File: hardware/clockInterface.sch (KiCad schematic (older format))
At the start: 9 parts, among them P501 CLOCK, SW501 SWITCH_INV, SW502 SWITCH_INV, SW503 SWITCH_INV, SW504 SWITCH_INV

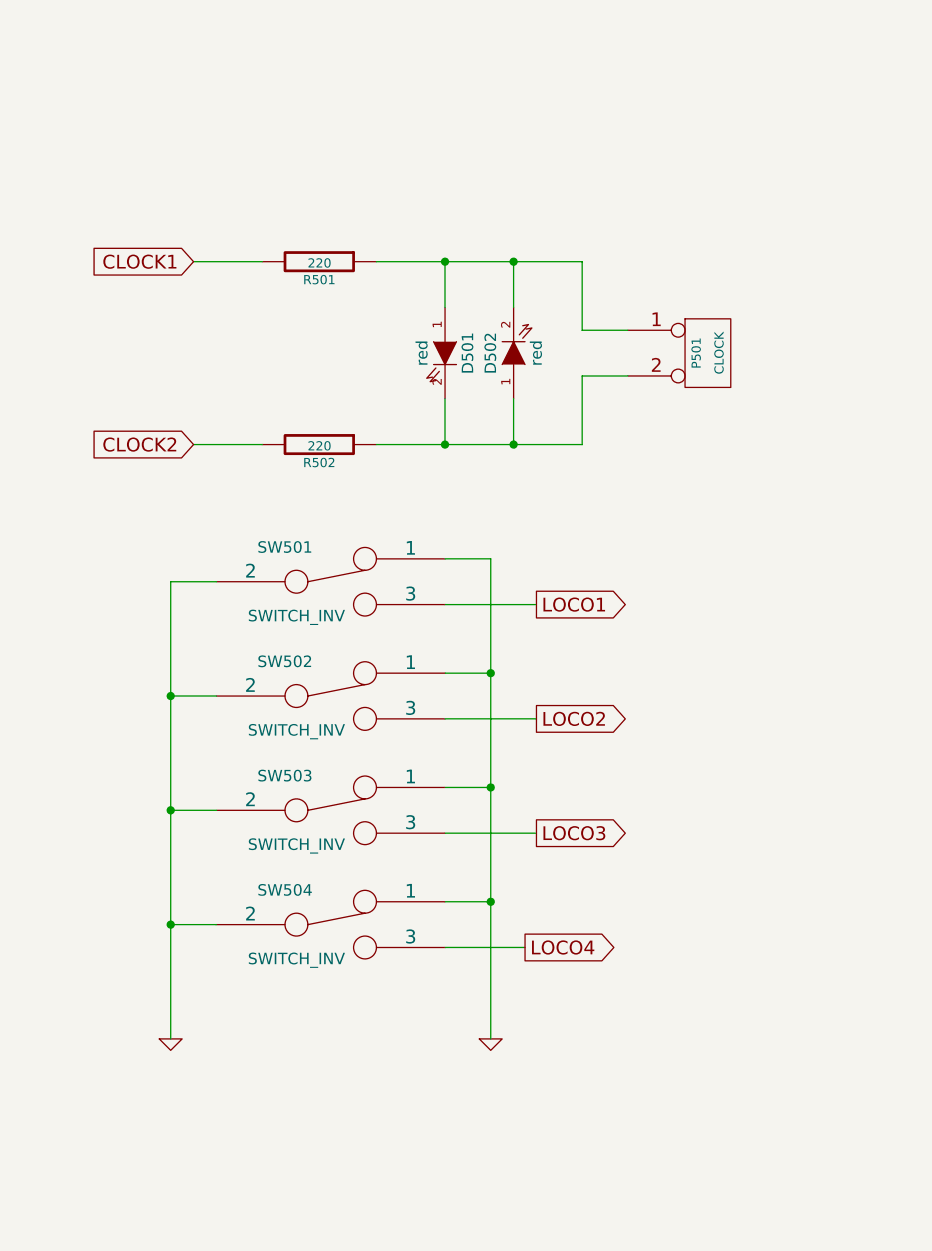
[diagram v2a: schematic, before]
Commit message: Change clock schematic and PCB
- Remove slide switches, replace with single push button
- Add status LED
- Re-add battery measurement connection

- Change PCB form factor to fit NewAgeEnclosures Compact AA housing
- Re-layout PCB
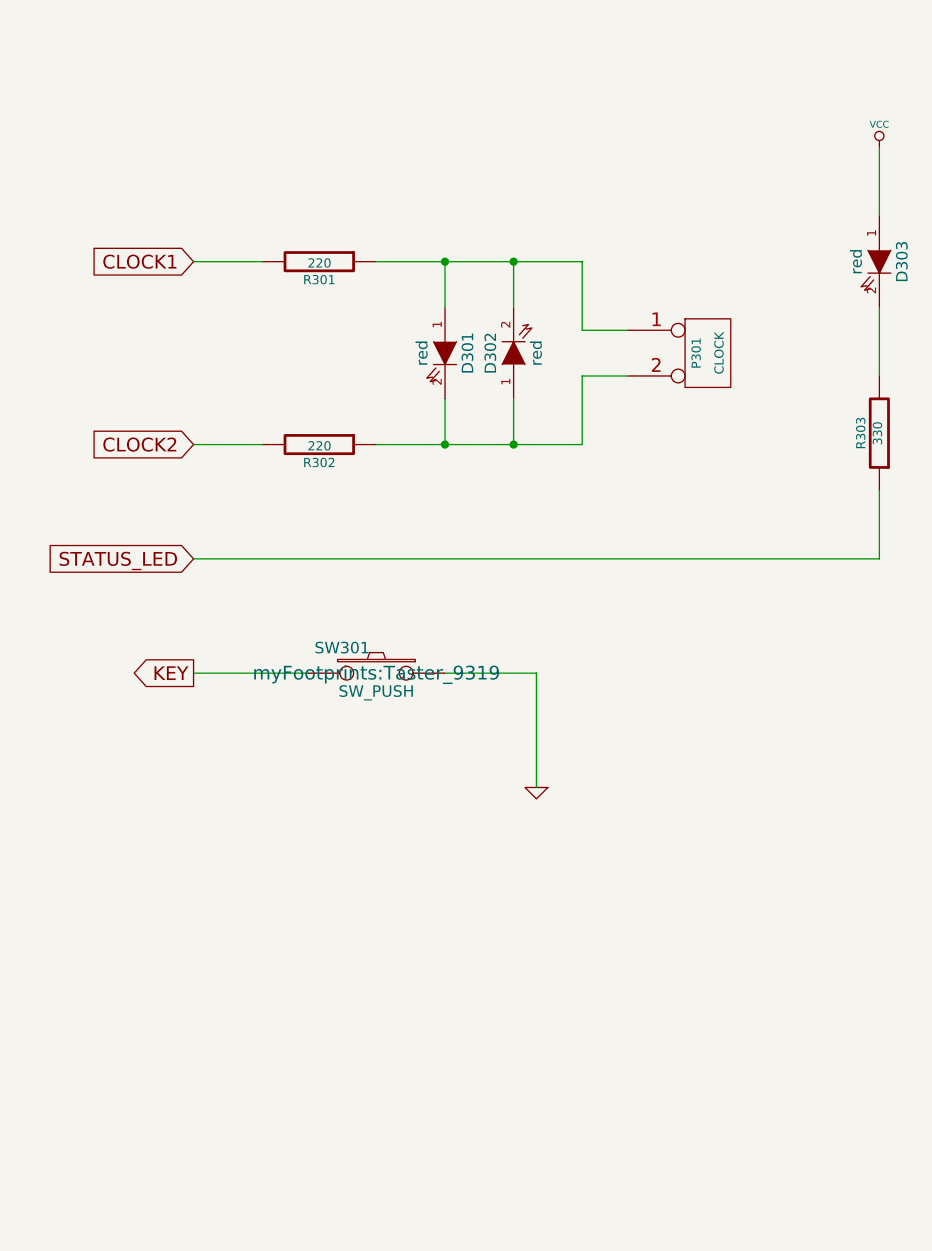
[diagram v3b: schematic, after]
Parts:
- removed SW501, SW502, SW503, SW504: SWITCH_INV, myFootprints:OS102011MS2Q, symbol SWITCH_INV
- added D303: red, myFootprints:LED_D3.0mm, symbol LED
- added R303: 330, Capacitors_SMD:C_0805_HandSoldering, symbol R
- added SW301: SW_PUSH, myFootprints:Taster_9319, symbol SW_PUSH
- renumbered D501 to D301, D502 to D302, P501 to P301, R501 to R301, R502 to R302
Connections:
- net GND: now also SW301.1
- new net: D303.2 (K), R303.2
- new net KEY: SW301.2
- new net STATUS_LED: R303.1
- new net VCC: D303.1 (A)
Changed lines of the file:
@@
 CLOCK2
 $Comp
-L R R501
+L R R301
 U 1 1 5A1291DD
 P 4450 2700
-F 0 "R501" V 4530 2700 40  0000 C CNN
+F 0 "R301" V 4530 2700 40  0000 C CNN
 F 1 "220" V 4457 2701 40  0000 C CNN
 F 2 "Capacitors_SMD:C_0805_HandSoldering" V 4380 2700 30  0001 C CNN
@@
 $EndComp
 $Comp
-L R R502
+L R R302
 U 1 1 5A12924F
 P 4450 3500
-F 0 "R502" V 4530 3500 40  0000 C CNN
+F 0 "R302" V 4530 3500 40  0000 C CNN
 F 1 "220" V 4457 3501 40  0000 C CNN
 F 2 "Capacitors_SMD:C_0805_HandSoldering" V 4380 3500 30  0001 C CNN
@@
 $EndComp
 $Comp
-L LED D501
+L LED D301
 U 1 1 5A12928F
 P 5000 3100
-F 0 "D501" H 5000 3200 50  0000 C CNN
+F 0 "D301" H 5000 3200 50  0000 C CNN
 F 1 "red" H 5000 3000 50  0000 C CNN
 F 2 "myFootprints:LED_D3.0mm" H 5000 3100 60  0001 C CNN
@@
 $EndComp
 $Comp
-L LED D502
+L LED D302
 U 1 1 5A129325
 P 5300 3100
-F 0 "D502" H 5300 3200 50  0000 C CNN
+F 0 "D302" H 5300 3200 50  0000 C CNN
 F 1 "red" H 5300 3000 50  0000 C CNN
 F 2 "myFootprints:LED_D3.0mm" H 5300 3100 60  0001 C CNN
@@
 $EndComp
 $Comp
-L CONN_2 P501
+L CONN_2 P301
 U 1 1 5A12938D
 P 6150 3100
-F 0 "P501" V 6100 3100 40  0000 C CNN
+F 0 "P301" V 6100 3100 40  0000 C CNN
 F 1 "CLOCK" V 6200 3100 40  0000 C CNN
 F 2 "myFootprints:AKL183-02" H 6150 3100 60  0001 C CNN
@@
 Connection ~ 5000 3500
 $Comp
-L SWITCH_INV SW501
-U 1 1 5A15342E
-P 4500 4100
-F 0 "SW501" H 4300 4250 50  0000 C CNN
-F 1 "SWITCH_INV" H 4350 3950 50  0000 C CNN
-F 2 "myFootprints:OS102011MS2Q" H 4500 4100 60  0001 C CNN
-F 3 "" H 4500 4100 60  0000 C CNN
-F 4 "611-OS102011MS2QN1" H 4500 4100 60  0001 C CNN "Mouser"
-	1    4500 4100
-	1    0    0    -1
+L GND #PWR018
+U 1 1 5A15360C
+P 5400 5000
+F 0 "#PWR018" H 5400 5000 30  0001 C CNN
+F 1 "GND" H 5400 4930 30  0001 C CNN
+F 2 "" H 5400 5000 60  0001 C CNN
+F 3 "" H 5400 5000 60  0001 C CNN
+	1    5400 5000
+	-1   0    0    -1
+$EndComp
+Wire Wire Line
+	5400 4500 5000 4500
+Text GLabel 3900 4500 0    60   Output ~ 0
+KEY
+Wire Wire Line
+	4400 4500 3900 4500
+Wire Wire Line
+	5400 4500 5400 5000
+$Comp
+L SW_PUSH SW301
+U 1 1 5C82A486
+P 4700 4500
+F 0 "SW301" H 4850 4610 50  0000 C CNN
+F 1 "SW_PUSH" H 4700 4420 50  0000 C CNN
+F 2 "myFootprints:Taster_9319" H 4700 4500 60  0000 C CNN
+F 3 "" H 4700 4500 60  0000 C CNN
+	1    4700 4500
+	-1   0    0    -1
 $EndComp
 $Comp
-L SWITCH_INV SW502
-U 1 1 5A15348B
-P 4500 4600
-F 0 "SW502" H 4300 4750 50  0000 C CNN
-F 1 "SWITCH_INV" H 4350 4450 50  0000 C CNN
-F 2 "myFootprints:OS102011MS2Q" H 4500 4600 60  0001 C CNN
-F 3 "" H 4500 4600 60  0000 C CNN
-F 4 "611-OS102011MS2QN1" H 4500 4600 60  0001 C CNN "Mouser"
-	1    4500 4600
-	1    0    0    -1
+L LED D303
+U 1 1 5C82A97E
+P 6900 2700
+F 0 "D303" H 6900 2800 50  0000 C CNN
+F 1 "red" H 6900 2600 50  0000 C CNN
+F 2 "myFootprints:LED_D3.0mm" H 6900 2700 60  0001 C CNN
+F 3 "" H 6900 2700 60  0000 C CNN
+F 4 "LED 3MM RT" H 6900 2700 60  0001 C CNN "Reichelt"
+	1    6900 2700
+	0    1    1    0
 $EndComp
 $Comp
-L SWITCH_INV SW503
-U 1 1 5A153526
-P 4500 5100
-F 0 "SW503" H 4300 5250 50  0000 C CNN
-F 1 "SWITCH_INV" H 4350 4950 50  0000 C CNN
-F 2 "myFootprints:OS102011MS2Q" H 4500 5100 60  0001 C CNN
-F 3 "" H 4500 5100 60  0000 C CNN
-F 4 "611-OS102011MS2QN1" H 4500 5100 60  0001 C CNN "Mouser"
-	1    4500 5100
-	1    0    0    -1
+L R R303
+U 1 1 5C82AAA2
+P 6900 3450
+F 0 "R303" V 6980 3450 40  0000 C CNN
+F 1 "330" V 6907 3451 40  0000 C CNN
+F 2 "Capacitors_SMD:C_0805_HandSoldering" V 6830 3450 30  0001 C CNN
+F 3 "" H 6900 3450 30  0000 C CNN
+F 4 "603-RC0805JR-07220RL" V 6900 3450 60  0001 C CNN "Mouser"
+	1    6900 3450
+	-1   0    0    1
 $EndComp
 $Comp
-L SWITCH_INV SW504
-U 1 1 5A1535A1
-P 4500 5600
-F 0 "SW504" H 4300 5750 50  0000 C CNN
-F 1 "SWITCH_INV" H 4350 5450 50  0000 C CNN
-F 2 "myFootprints:OS102011MS2Q" H 4500 5600 60  0001 C CNN
-F 3 "" H 4500 5600 60  0000 C CNN
-F 4 "611-OS102011MS2QN1" H 4500 5600 60  0001 C CNN "Mouser"
-	1    4500 5600
-	1    0    0    -1
-$EndComp
-$Comp
-L GND #PWR017
-U 1 1 5A15360C
-P 3800 6100
-F 0 "#PWR017" H 3800 6100 30  0001 C CNN
-F 1 "GND" H 3800 6030 30  0001 C CNN
-F 2 "" H 3800 6100 60  0001 C CNN
-F 3 "" H 3800 6100 60  0001 C CNN
-	1    3800 6100
-	1    0    0    -1
-$EndComp
-$Comp
-L GND #PWR018
-U 1 1 5A15363B
-P 5200 6100
-F 0 "#PWR018" H 5200 6100 30  0001 C CNN
-F 1 "GND" H 5200 6030 30  0001 C CNN
-F 2 "" H 5200 6100 60  0001 C CNN
-F 3 "" H 5200 6100 60  0001 C CNN
-	1    5200 6100
+L VCC #PWR019
+U 1 1 5C82ABFF
+P 6900 2200
+F 0 "#PWR019" H 6900 2300 30  0001 C CNN
+F 1 "VCC" H 6900 2300 30  0000 C CNN
+F 2 "" H 6900 2200 60  0001 C CNN
+F 3 "" H 6900 2200 60  0001 C CNN
+	1    6900 2200
 	1    0    0    -1
 $EndComp
 Wire Wire Line
-	5200 6100 5200 4000
+	6900 2200 6900 2500
 Wire Wire Line
-	5200 4000 5000 4000
+	6900 2900 6900 3200
 Wire Wire Line
-	5000 4500 5200 4500
-Connection ~ 5200 4500
+	6900 3700 6900 4000
 Wire Wire Line
-	5000 5000 5200 5000
-Connection ~ 5200 5000
-Wire Wire Line
-	5000 5500 5200 5500
-Connection ~ 5200 5500
-Wire Wire Line
-	3800 4100 3800 6100
-Wire Wire Line
-	3800 5600 4000 5600
-Wire Wire Line
-	3800 5100 4000 5100
-Connection ~ 3800 5600
-Wire Wire Line
-	3800 4600 4000 4600
-Connection ~ 3800 5100
-Wire Wire Line
-	3800 4100 4000 4100
-Connection ~ 3800 4600
-Text GLabel 5400 4200 2    60   Output ~ 0
-LOCO1
-Text GLabel 5400 4700 2    60   Output ~ 0
-LOCO2
-Text GLabel 5400 5200 2    60   Output ~ 0
-LOCO3
-Text GLabel 5350 5700 2    60   Output ~ 0
-LOCO4
-Wire Wire Line
-	5400 4700 5000 4700
-Wire Wire Line
-	5000 4200 5400 4200
-Wire Wire Line
-	5400 5200 5000 5200
-Wire Wire Line
-	5000 5700 5350 5700
+	6900 4000 3900 4000
+Text GLabel 3900 4000 0    60   Input ~ 0
+STATUS_LED
 $EndSCHEMATC

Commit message: Changed PCB and code to closer match first PCB
- Add battery measurement resistors
- Move key, status LED and clock I/O-pins around to match first PCB
  (except for CLOCK1 which is on low power pin in first version)
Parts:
- SW301: Mouser (none) -> 611-PTS645SM13SMTR92
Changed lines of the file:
@@
 Connection ~ 5000 3500
 $Comp
-L GND #PWR018
+L GND #PWR019
 U 1 1 5A15360C
 P 5400 5000
-F 0 "#PWR018" H 5400 5000 30  0001 C CNN
+F 0 "#PWR019" H 5400 5000 30  0001 C CNN
 F 1 "GND" H 5400 4930 30  0001 C CNN
 F 2 "" H 5400 5000 60  0001 C CNN
@@
 F 2 "myFootprints:Taster_9319" H 4700 4500 60  0000 C CNN
 F 3 "" H 4700 4500 60  0000 C CNN
+F 4 "611-PTS645SM13SMTR92" H 4700 4500 60  0001 C CNN "Mouser"
 	1    4700 4500
 	-1   0    0    -1
@@
 $EndComp
 $Comp
-L VCC #PWR019
+L VCC #PWR020
 U 1 1 5C82ABFF
 P 6900 2200
-F 0 "#PWR019" H 6900 2300 30  0001 C CNN
+F 0 "#PWR020" H 6900 2300 30  0001 C CNN
 F 1 "VCC" H 6900 2300 30  0000 C CNN
 F 2 "" H 6900 2200 60  0001 C CNN

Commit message: Added more keys to the PCB for adjusting the time
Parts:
- added SW302, SW303, SW304: SW_PUSH, myFootprints:Taster_9319, symbol SW_PUSH
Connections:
- net GND: now also SW302.1, SW303.1, SW304.1
- net KEY: now also SW304.2; no longer SW301.2
- new net KEY_CONF: SW301.2
- new net KEY_HOUR: SW302.2
- new net KEY_MINUTE: SW303.2
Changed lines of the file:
@@
 L GND #PWR019
 U 1 1 5A15360C
-P 5400 5000
-F 0 "#PWR019" H 5400 5000 30  0001 C CNN
-F 1 "GND" H 5400 4930 30  0001 C CNN
-F 2 "" H 5400 5000 60  0001 C CNN
-F 3 "" H 5400 5000 60  0001 C CNN
-	1    5400 5000
+P 5400 6900
+F 0 "#PWR019" H 5400 6900 30  0001 C CNN
+F 1 "GND" H 5400 6830 30  0001 C CNN
+F 2 "" H 5400 6900 60  0001 C CNN
+F 3 "" H 5400 6900 60  0001 C CNN
+	1    5400 6900
 	-1   0    0    -1
 $EndComp
@@
 	5400 4500 5000 4500
 Text GLabel 3900 4500 0    60   Output ~ 0
-KEY
+KEY_CONF
 Wire Wire Line
 	4400 4500 3900 4500
 Wire Wire Line
-	5400 4500 5400 5000
+	5400 4500 5400 6900
 $Comp
 L SW_PUSH SW301
@@
 Text GLabel 3900 4000 0    60   Input ~ 0
 STATUS_LED
+Wire Wire Line
+	5400 4900 5000 4900
+Text GLabel 3900 4900 0    60   Output ~ 0
+KEY_HOUR
+Wire Wire Line
+	4400 4900 3900 4900
+$Comp
+L SW_PUSH SW302
+U 1 1 5CA9E853
+P 4700 4900
+F 0 "SW302" H 4850 5010 50  0000 C CNN
+F 1 "SW_PUSH" H 4700 4820 50  0000 C CNN
+F 2 "myFootprints:Taster_9319" H 4700 4900 60  0000 C CNN
+F 3 "" H 4700 4900 60  0000 C CNN
+F 4 "611-PTS645SM13SMTR92" H 4700 4900 60  0001 C CNN "Mouser"
+	1    4700 4900
+	-1   0    0    -1
+$EndComp
+Wire Wire Line
+	5400 5300 5000 5300
+Text GLabel 3900 5300 0    60   Output ~ 0
+KEY_MINUTE
+Wire Wire Line
+	4400 5300 3900 5300
+$Comp
+L SW_PUSH SW303
+U 1 1 5CA9E95A
+P 4700 5300
+F 0 "SW303" H 4850 5410 50  0000 C CNN
+F 1 "SW_PUSH" H 4700 5220 50  0000 C CNN
+F 2 "myFootprints:Taster_9319" H 4700 5300 60  0000 C CNN
+F 3 "" H 4700 5300 60  0000 C CNN
+F 4 "611-PTS645SM13SMTR92" H 4700 5300 60  0001 C CNN "Mouser"
+	1    4700 5300
+	-1   0    0    -1
+$EndComp
+Wire Wire Line
+	5400 5700 5000 5700
+Text GLabel 3900 5700 0    60   Output ~ 0
+KEY
+Wire Wire Line
+	4400 5700 3900 5700
+$Comp
+L SW_PUSH SW304
+U 1 1 5CA9E9B6
+P 4700 5700
+F 0 "SW304" H 4850 5810 50  0000 C CNN
+F 1 "SW_PUSH" H 4700 5620 50  0000 C CNN
+F 2 "myFootprints:Taster_9319" H 4700 5700 60  0000 C CNN
+F 3 "" H 4700 5700 60  0000 C CNN
+F 4 "611-PTS645SM13SMTR92" H 4700 5700 60  0001 C CNN "Mouser"
+	1    4700 5700
+	-1   0    0    -1
+$EndComp
+Connection ~ 5400 4900
+Connection ~ 5400 5300
+Connection ~ 5400 5700
 $EndSCHEMATC

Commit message: Add second clock output...
...while removing (so far) unused key
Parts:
- removed SW304: SW_PUSH, myFootprints:Taster_9319, symbol SW_PUSH
- added D304, D305: red, myFootprints:LED_D3.0mm, symbol LED
- added P302: CLOCK2, myFootprints:AKL183-02, symbol CONN_2
- added R304, R305: 220, Capacitors_SMD:C_0805_HandSoldering, symbol R
- D303: value red -> green
- P301: value CLOCK -> CLOCK1
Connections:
- new net: D304.1 (A), D305.2 (K), P302.1 (P1), R304.1
- new net: D304.2 (K), D305.1 (A), P302.2 (PM), R305.1
- new net CLOCK3: R304.2
- new net CLOCK4: R305.2
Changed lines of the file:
@@
 EESchema Schematic File Version 2
+LIBS:wfred_loconet_clock-rescue
 LIBS:power
 LIBS:device
@@
 P 6150 3100
 F 0 "P301" V 6100 3100 40  0000 C CNN
-F 1 "CLOCK" V 6200 3100 40  0000 C CNN
+F 1 "CLOCK1" V 6200 3100 40  0000 C CNN
 F 2 "myFootprints:AKL183-02" H 6150 3100 60  0001 C CNN
 F 3 "" H 6150 3100 60  0001 C CNN
@@
 Connection ~ 5000 3500
 $Comp
-L GND #PWR019
+L GND #PWR020
 U 1 1 5A15360C
 P 5400 6900
-F 0 "#PWR019" H 5400 6900 30  0001 C CNN
+F 0 "#PWR020" H 5400 6900 30  0001 C CNN
 F 1 "GND" H 5400 6830 30  0001 C CNN
 F 2 "" H 5400 6900 60  0001 C CNN
@@
 Wire Wire Line
 	4400 4500 3900 4500
-Wire Wire Line
-	5400 4500 5400 6900
 $Comp
 L SW_PUSH SW301
@@
 P 6900 2700
 F 0 "D303" H 6900 2800 50  0000 C CNN
-F 1 "red" H 6900 2600 50  0000 C CNN
+F 1 "green" H 6900 2600 50  0000 C CNN
 F 2 "myFootprints:LED_D3.0mm" H 6900 2700 60  0001 C CNN
 F 3 "" H 6900 2700 60  0000 C CNN
@@
 $EndComp
 $Comp
-L VCC #PWR020
+L VCC #PWR021
 U 1 1 5C82ABFF
 P 6900 2200
-F 0 "#PWR020" H 6900 2300 30  0001 C CNN
+F 0 "#PWR021" H 6900 2300 30  0001 C CNN
 F 1 "VCC" H 6900 2300 30  0000 C CNN
 F 2 "" H 6900 2200 60  0001 C CNN
@@
 	-1   0    0    -1
 $EndComp
-Wire Wire Line
-	5400 5700 5000 5700
-Text GLabel 3900 5700 0    60   Output ~ 0
-KEY
-Wire Wire Line
-	4400 5700 3900 5700
-$Comp
-L SW_PUSH SW304
-U 1 1 5CA9E9B6
-P 4700 5700
-F 0 "SW304" H 4850 5810 50  0000 C CNN
-F 1 "SW_PUSH" H 4700 5620 50  0000 C CNN
-F 2 "myFootprints:Taster_9319" H 4700 5700 60  0000 C CNN
-F 3 "" H 4700 5700 60  0000 C CNN
-F 4 "611-PTS645SM13SMTR92" H 4700 5700 60  0001 C CNN "Mouser"
-	1    4700 5700
-	-1   0    0    -1
-$EndComp
 Connection ~ 5400 4900
 Connection ~ 5400 5300
-Connection ~ 5400 5700
+Text GLabel 3900 1700 0    60   Input ~ 0
+CLOCK3
+Text GLabel 3900 2500 0    60   Input ~ 0
+CLOCK4
+$Comp
+L R R304
+U 1 1 5D44BDE6
+P 4450 1700
+F 0 "R304" V 4530 1700 40  0000 C CNN
+F 1 "220" V 4457 1701 40  0000 C CNN
+F 2 "Capacitors_SMD:C_0805_HandSoldering" V 4380 1700 30  0001 C CNN
+F 3 "" H 4450 1700 30  0000 C CNN
+F 4 "603-RC0805JR-07220RL" V 4450 1700 60  0001 C CNN "Mouser"
+	1    4450 1700
+	0    1    1    0
+$EndComp
+$Comp
+L R R305
+U 1 1 5D44BDED
+P 4450 2500
+F 0 "R305" V 4530 2500 40  0000 C CNN
+F 1 "220" V 4457 2501 40  0000 C CNN
+F 2 "Capacitors_SMD:C_0805_HandSoldering" V 4380 2500 30  0001 C CNN
+F 3 "" H 4450 2500 30  0000 C CNN
+F 4 "603-RC0805JR-07220RL" V 4450 2500 60  0001 C CNN "Mouser"
+	1    4450 2500
+	0    1    1    0
+$EndComp
+$Comp
+L LED D304
+U 1 1 5D44BDF4
+P 5000 2100
+F 0 "D304" H 5000 2200 50  0000 C CNN
+F 1 "red" H 5000 2000 50  0000 C CNN
+F 2 "myFootprints:LED_D3.0mm" H 5000 2100 60  0001 C CNN
+F 3 "" H 5000 2100 60  0000 C CNN
+F 4 "LED 3MM RT" H 5000 2100 60  0001 C CNN "Reichelt"
+	1    5000 2100
+	0    1    1    0
+$EndComp
+$Comp
+L LED D305
+U 1 1 5D44BDFB
+P 5300 2100
+F 0 "D305" H 5300 2200 50  0000 C CNN
+F 1 "red" H 5300 2000 50  0000 C CNN
+F 2 "myFootprints:LED_D3.0mm" H 5300 2100 60  0001 C CNN
+F 3 "" H 5300 2100 60  0000 C CNN
+F 4 "LED 3MM RT" H 5300 2100 60  0001 C CNN "Reichelt"
+	1    5300 2100
+	0    -1   -1   0
+$EndComp
+$Comp
+L CONN_2 P302
+U 1 1 5D44BE02
+P 6150 2100
+F 0 "P302" V 6100 2100 40  0000 C CNN
+F 1 "CLOCK2" V 6200 2100 40  0000 C CNN
+F 2 "myFootprints:AKL183-02" H 6150 2100 60  0001 C CNN
+F 3 "" H 6150 2100 60  0001 C CNN
+F 4 "AKL182-02 + AKL169-02" V 6150 2100 60  0001 C CNN "Reichelt"
+	1    6150 2100
+	1    0    0    -1
+$EndComp
+Wire Wire Line
+	3900 1700 4200 1700
+Wire Wire Line
+	4700 1700 5600 1700
+Wire Wire Line
+	5600 1700 5600 2000
+Wire Wire Line
+	5600 2000 5800 2000
+Wire Wire Line
+	5300 1900 5300 1700
+Connection ~ 5300 1700
+Wire Wire Line
+	5000 1900 5000 1700
+Connection ~ 5000 1700
+Wire Wire Line
+	3900 2500 4200 2500
+Wire Wire Line
+	4700 2500 5600 2500
+Wire Wire Line
+	5600 2500 5600 2200
+Wire Wire Line
+	5600 2200 5800 2200
+Wire Wire Line
+	5300 2300 5300 2500
+Connection ~ 5300 2500
+Wire Wire Line
+	5000 2300 5000 2500
+Connection ~ 5000 2500
+Wire Wire Line
+	5400 4500 5400 6900
 $EndSCHEMATC
